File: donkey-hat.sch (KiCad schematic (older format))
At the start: 63 parts, among them J1 5V, J10 8, J11 9, J12 10, J13 11, J14 NEOPIXEL, J15 MPU-9250, J16 4, J17 5, J18 6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

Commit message: Schematic updated
PWM pins reduced.
level shifter removed.
Ultrasonic model changed.
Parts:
- removed C5, C6: 100nF, Capacitor_SMD:C_0603_1608Metric_Pad1.05x0.95mm_HandSolder, symbol Device:C
- removed J10: 8, Connector_PinHeader_2.54mm:PinHeader_1x03_P2.54mm_Vertical, symbol Connector:Conn_01x03_Male
- removed J11: 9, Connector_PinHeader_2.54mm:PinHeader_1x03_P2.54mm_Vertical, symbol Connector:Conn_01x03_Male
- removed J12: 10, Connector_PinHeader_2.54mm:PinHeader_1x03_P2.54mm_Vertical, symbol Connector:Conn_01x03_Male
- removed J13: 11, Connector_PinHeader_2.54mm:PinHeader_1x03_P2.54mm_Vertical, symbol Connector:Conn_01x03_Male
- removed J20: 12, Connector_PinHeader_2.54mm:PinHeader_1x03_P2.54mm_Vertical, symbol Connector:Conn_01x03_Male
- removed J21: 13, Connector_PinHeader_2.54mm:PinHeader_1x03_P2.54mm_Vertical, symbol Connector:Conn_01x03_Male
- removed J22: 14, Connector_PinHeader_2.54mm:PinHeader_1x03_P2.54mm_Vertical, symbol Connector:Conn_01x03_Male
- removed J23: 15, Connector_PinHeader_2.54mm:PinHeader_1x03_P2.54mm_Vertical, symbol Connector:Conn_01x03_Male
- removed J3: ULTRA_0, Connector_PinHeader_2.54mm:PinHeader_1x03_P2.54mm_Vertical, symbol Connector_Generic:Conn_01x03
- removed J4: ULTRA_1, Connector_PinHeader_2.54mm:PinHeader_1x03_P2.54mm_Vertical, symbol Connector_Generic:Conn_01x03
- removed J5: TXB0108, Package_SO:TSSOP-20_4.4x6.5mm_P0.65mm, symbol Connector_Generic:Conn_02x10_Counter_Clockwise
- removed JP10, JP11, JP12, JP13, JP8, JP9: LINK, libs:SolderJumper-2_small, symbol Jumper:SolderJumper_2_Open
- removed RN3, RN4: 220_Pack04, Resistor_SMD:R_Array_Convex_4x0603, symbol Device:R_Pack04
- added J3: ULTRA_0, Connector_PinSocket_2.54mm:PinSocket_1x04_P2.54mm_Vertical, symbol Connector_Generic:Conn_01x04
- added J4: ULTRA_1, Connector_PinSocket_2.54mm:PinSocket_1x04_P2.54mm_Vertical, symbol Connector_Generic:Conn_01x04
- added R3, R5: 330, Resistor_SMD:R_0603_1608Metric_Pad1.05x0.95mm_HandSolder, symbol Device:R
- added R4, R6: 470, Resistor_SMD:R_0603_1608Metric_Pad1.05x0.95mm_HandSolder, symbol Device:R
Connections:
- net labels added: ECHO, TRIG
- net labels removed: GPIO18_5, GPIO24_5, GPIO25_5, INT, SCL_5, SDA_5
- wire segments 366 -> 281
- no-connect marks 13 -> 7
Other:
- note added: "Accelerometer"
- moved on the sheet: J15

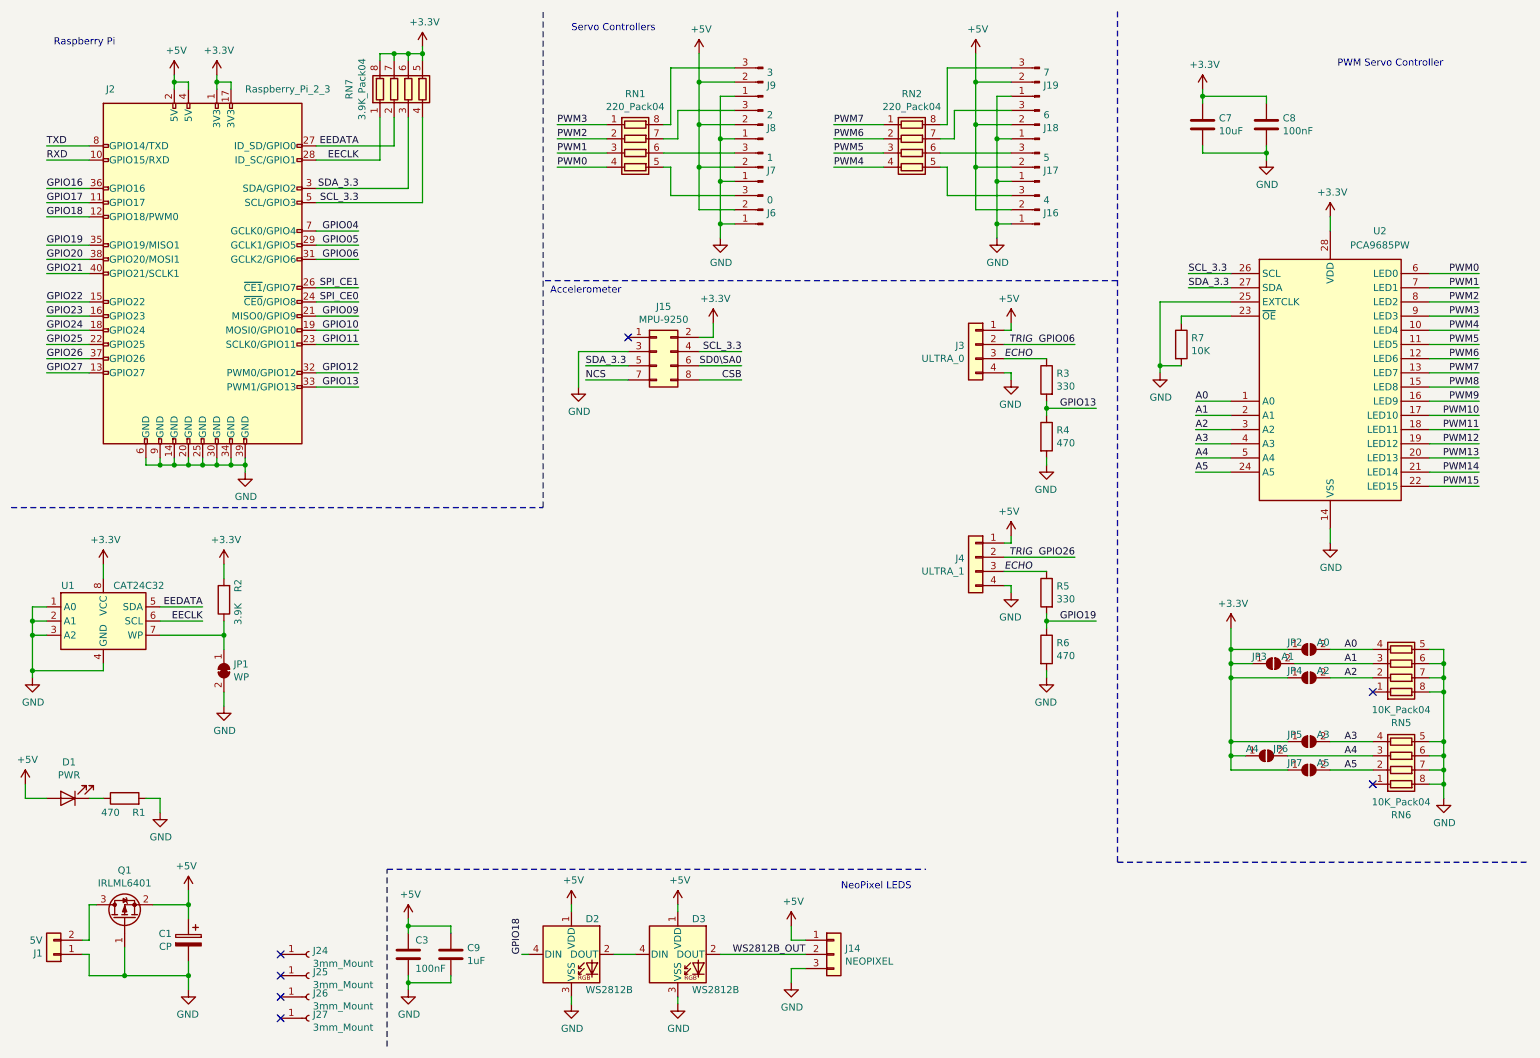
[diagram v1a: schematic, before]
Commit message: Resistor Bank for i2c is causing issues.
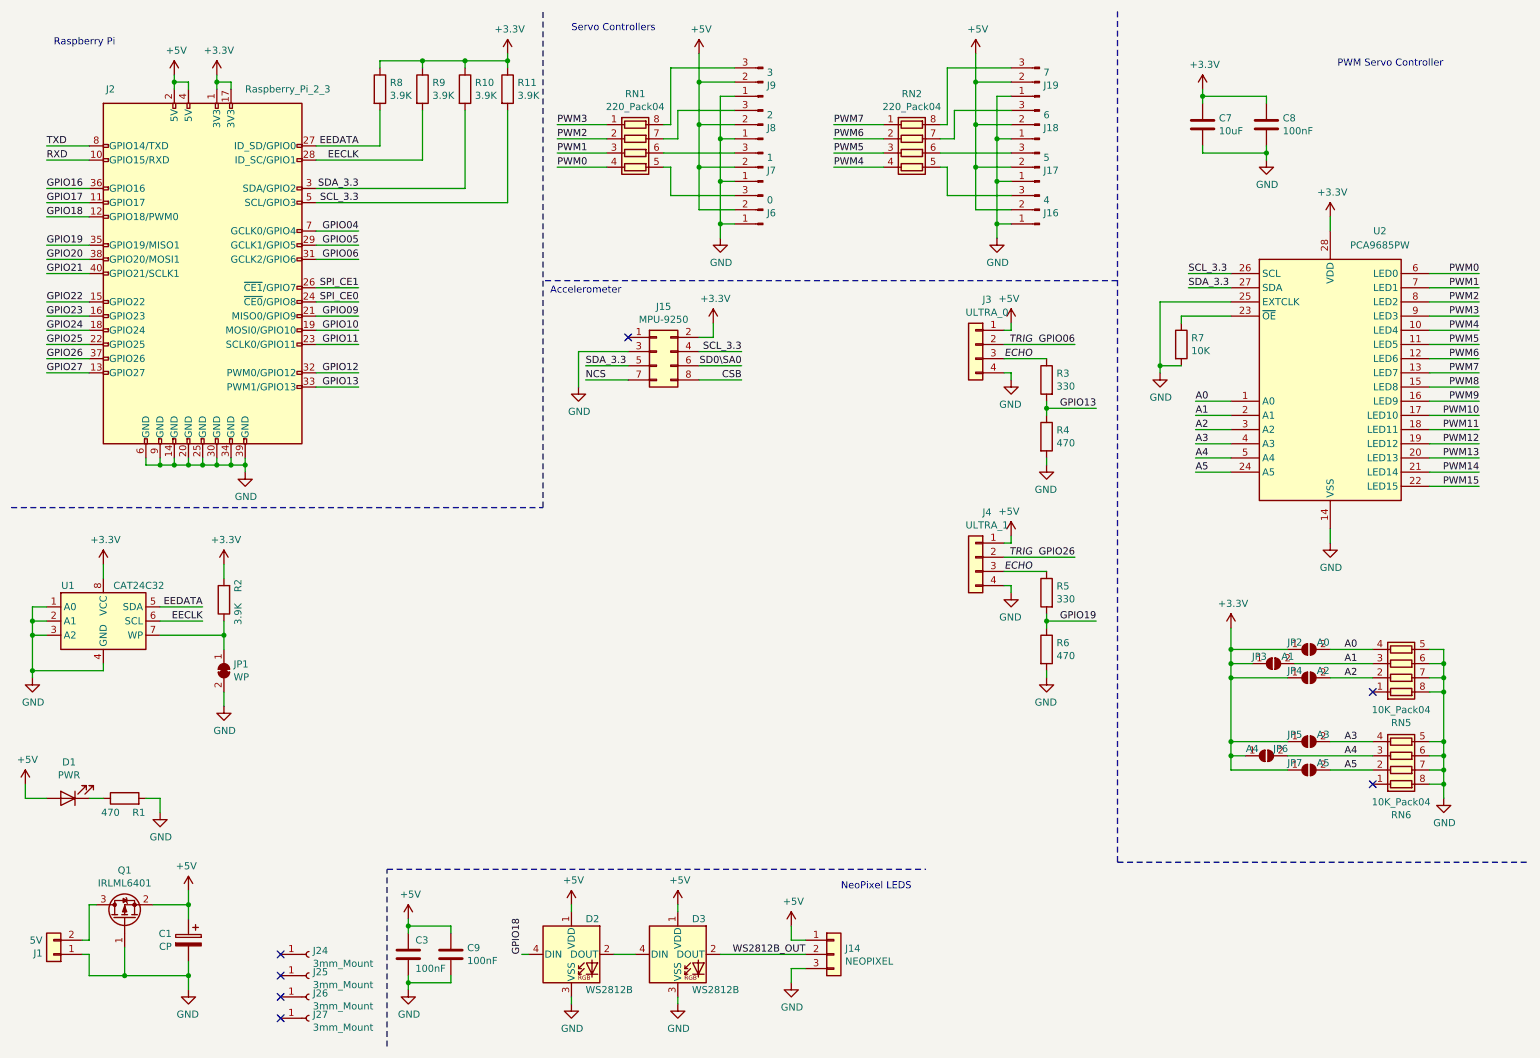
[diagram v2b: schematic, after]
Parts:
- removed RN7: 3.9K_Pack04, Resistor_SMD:R_Array_Convex_4x0603, symbol Device:R_Pack04
- added R10, R11, R8, R9: 3.9K, Resistor_SMD:R_0603_1608Metric_Pad1.05x0.95mm_HandSolder, symbol Device:R
- C9: value 1uF -> 100nF
- J3, J4: Link (none) -> https://tronixlabs.com.au/sensors/distance/ultrasonic/ultra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
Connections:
- net +3V3: now also R10.1, R11.1, R8.1, R9.1
- net EECLK: now also R9.2
- net EEDATA: now also R8.2
- net SCL_3.3: now also R11.2
- net SDA_3.3: now also R10.2
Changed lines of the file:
@@
 L power:+3.3V #PWR0111
 U 1 1 5C049CFC
-P 3400 750
-F 0 "#PWR0111" H 3400 600 50  0001 C CNN
-F 1 "+3.3V" H 3415 923 50  0000 C CNN
-F 2 "" H 3400 750 50  0001 C CNN
-F 3 "" H 3400 750 50  0001 C CNN
-	1    3400 750
+P 4000 800
+F 0 "#PWR0111" H 4000 650 50  0001 C CNN
+F 1 "+3.3V" H 4015 973 50  0000 C CNN
+F 2 "" H 4000 800 50  0001 C CNN
+F 3 "" H 4000 800 50  0001 C CNN
+	1    4000 800
 	1    0    0    -1
 $EndComp
@@
 Wire Wire Line
 	6100 7150 5500 7150
-Wire Wire Line
-	2650 1550 3100 1550
-Wire Wire Line
-	2650 1750 3300 1750
-Wire Wire Line
-	2650 1850 3400 1850
 $Comp
 L Device:C C3
@@
 A5
 $Comp
-L Device:R_Pack04 RN7
-U 1 1 5CAD6C78
-P 3300 1050
-F 0 "RN7" V 2883 1050 50  0000 C CNN
-F 1 "3.9K_Pack04" V 2974 1050 50  0000 C CNN
-F 2 "Resistor_SMD:R_Array_Convex_4x0603" V 3575 1050 50  0001 C CNN
-F 3 "~" H 3300 1050 50  0001 C CNN
-F 4 "https://www.aliexpress.com/item/200PCS-0603-2X4-220R-220-ohm-Marking-221-SMD-Network-Resistor-array-0603-8P4R-2-4P/32845505270.html?spm=2114.search0104.3.35.c74a11b9SNycSm&ws_ab_test=searchweb0_0,searchweb201602_2_10065_10068_10130_10547_319_317_10548_10696_453_10084_454_10083_10618_10307_537_536_10131_10132_10133_10059_10884_10887_100031_321_322_10103,searchweb201603_51,ppcSwitch_0&algo_expid=516fab08-5bb7-441c-804a-744d42f8303d-5&algo_pvid=516fab08-5bb7-441c-804a-744d42f8303d" V 3300 1050 50  0001 C CNN "Link"
-	1    3300 1050
-	1    0    0    -1
-$EndComp
-Wire Wire Line
-	3100 850  3100 800
-Wire Wire Line
-	3100 800  3200 800
-Wire Wire Line
-	3400 800  3400 750
-Wire Wire Line
-	3400 850  3400 800
-Connection ~ 3400 800
-Wire Wire Line
-	3300 850  3300 800
-Connection ~ 3300 800
-Wire Wire Line
-	3300 800  3400 800
-Wire Wire Line
-	3200 850  3200 800
-Connection ~ 3200 800
-Wire Wire Line
-	3200 800  3300 800
-Wire Wire Line
-	3300 1250 3300 1750
-Wire Wire Line
-	3400 1250 3400 1850
-$Comp
 L Device:C C9
 U 1 1 5CC83074
 P 3600 7150
 F 0 "C9" H 3715 7196 50  0000 L CNN
-F 1 "1uF" H 3715 7105 50  0000 L CNN
+F 1 "100nF" H 3715 7105 50  0000 L CNN
 F 2 "Capacitor_SMD:C_0603_1608Metric_Pad1.05x0.95mm_HandSolder" H 3638 7000 50  0001 C CNN
 F 3 "~" H 3600 7150 50  0001 C CNN
@@
 	3300 7350 3300 7300
 Wire Wire Line
-	3200 1450 3200 1250
-Wire Wire Line
-	2650 1450 3200 1450
-Wire Wire Line
-	3100 1250 3100 1550
+	2650 1450 3100 1450
 $Comp
 L Connector_Generic:Conn_02x04_Odd_Even J15
@@
 U 1 1 5C1BDC5B
 P 7300 4350
-F 0 "J4" H 7379 4342 50  0000 L CNN
-F 1 "ULTRA_1" H 7379 4251 50  0000 L CNN
+F 0 "J4" H 7220 4667 50  0000 C CNN
+F 1 "ULTRA_1" H 7220 4576 50  0000 C CNN
 F 2 "Connector_PinSocket_2.54mm:PinSocket_1x04_P2.54mm_Vertical" H 7300 4350 50  0001 C CNN
 F 3 "~" H 7300 4350 50  0001 C CNN
+F 4 "https://tronixlabs.com.au/sensors/distance/ultrasonic/ultrasonic-distance-sensor-module-hc-sr04-2-450-cm-australia/" H 7300 4350 50  0001 C CNN "Link"
 	1    7300 4350
 	-1   0    0    -1
@@
 U 1 1 5C210D5B
 P 7300 2850
-F 0 "J3" H 7379 2842 50  0000 L CNN
-F 1 "ULTRA_0" H 7379 2751 50  0000 L CNN
+F 0 "J3" H 7220 3167 50  0000 C CNN
+F 1 "ULTRA_0" H 7220 3076 50  0000 C CNN
 F 2 "Connector_PinSocket_2.54mm:PinSocket_1x04_P2.54mm_Vertical" H 7300 2850 50  0001 C CNN
 F 3 "~" H 7300 2850 50  0001 C CNN
+F 4 "https://tronixlabs.com.au/sensors/distance/ultrasonic/ultrasonic-distance-sensor-module-hc-sr04-2-450-cm-australia/" H 7300 2850 50  0001 C CNN "Link"
 	1    7300 2850
 	-1   0    0    -1
@@
 Wire Wire Line
 	7800 5200 7800 5150
+$Comp
+L Device:R R8
+U 1 1 5C3CDDE7
+P 3100 1050
+F 0 "R8" H 3170 1096 50  0000 L CNN
+F 1 "3.9K" H 3170 1005 50  0000 L CNN
+F 2 "Resistor_SMD:R_0603_1608Metric_Pad1.05x0.95mm_HandSolder" V 3030 1050 50  0001 C CNN
+F 3 "~" H 3100 1050 50  0001 C CNN
+	1    3100 1050
+	1    0    0    -1
+$EndComp
+$Comp
+L Device:R R9
+U 1 1 5C40A918
+P 3400 1050
+F 0 "R9" H 3470 1096 50  0000 L CNN
+F 1 "3.9K" H 3470 1005 50  0000 L CNN
+F 2 "Resistor_SMD:R_0603_1608Metric_Pad1.05x0.95mm_HandSolder" V 3330 1050 50  0001 C CNN
+F 3 "~" H 3400 1050 50  0001 C CNN
+	1    3400 1050
+	1    0    0    -1
+$EndComp
+$Comp
+L Device:R R10
+U 1 1 5C432542
+P 3700 1050
+F 0 "R10" H 3770 1096 50  0000 L CNN
+F 1 "3.9K" H 3770 1005 50  0000 L CNN
+F 2 "Resistor_SMD:R_0603_1608Metric_Pad1.05x0.95mm_HandSolder" V 3630 1050 50  0001 C CNN
+F 3 "~" H 3700 1050 50  0001 C CNN
+	1    3700 1050
+	1    0    0    -1
+$EndComp
+$Comp
+L Device:R R11
+U 1 1 5C432548
+P 4000 1050
+F 0 "R11" H 4070 1096 50  0000 L CNN
+F 1 "3.9K" H 4070 1005 50  0000 L CNN
+F 2 "Resistor_SMD:R_0603_1608Metric_Pad1.05x0.95mm_HandSolder" V 3930 1050 50  0001 C CNN
+F 3 "~" H 4000 1050 50  0001 C CNN
+	1    4000 1050
+	1    0    0    -1
+$EndComp
+Wire Wire Line
+	3400 1550 3400 1200
+Wire Wire Line
+	2650 1550 3400 1550
+Wire Wire Line
+	3100 1450 3100 1200
+Wire Wire Line
+	3100 900  3100 850
+Wire Wire Line
+	3100 850  3400 850
+Wire Wire Line
+	4000 850  4000 900
+Wire Wire Line
+	3400 900  3400 850
+Connection ~ 3400 850
+Wire Wire Line
+	3400 850  3700 850
+Wire Wire Line
+	3700 850  3700 900
+Connection ~ 3700 850
+Wire Wire Line
+	3700 850  4000 850
+Wire Wire Line
+	3700 1200 3700 1750
+Wire Wire Line
+	2650 1750 3700 1750
+Wire Wire Line
+	4000 1850 4000 1200
+Wire Wire Line
+	2650 1850 4000 1850
+Wire Wire Line
+	4000 800  4000 850
+Connection ~ 4000 850
 $EndSCHEMATC

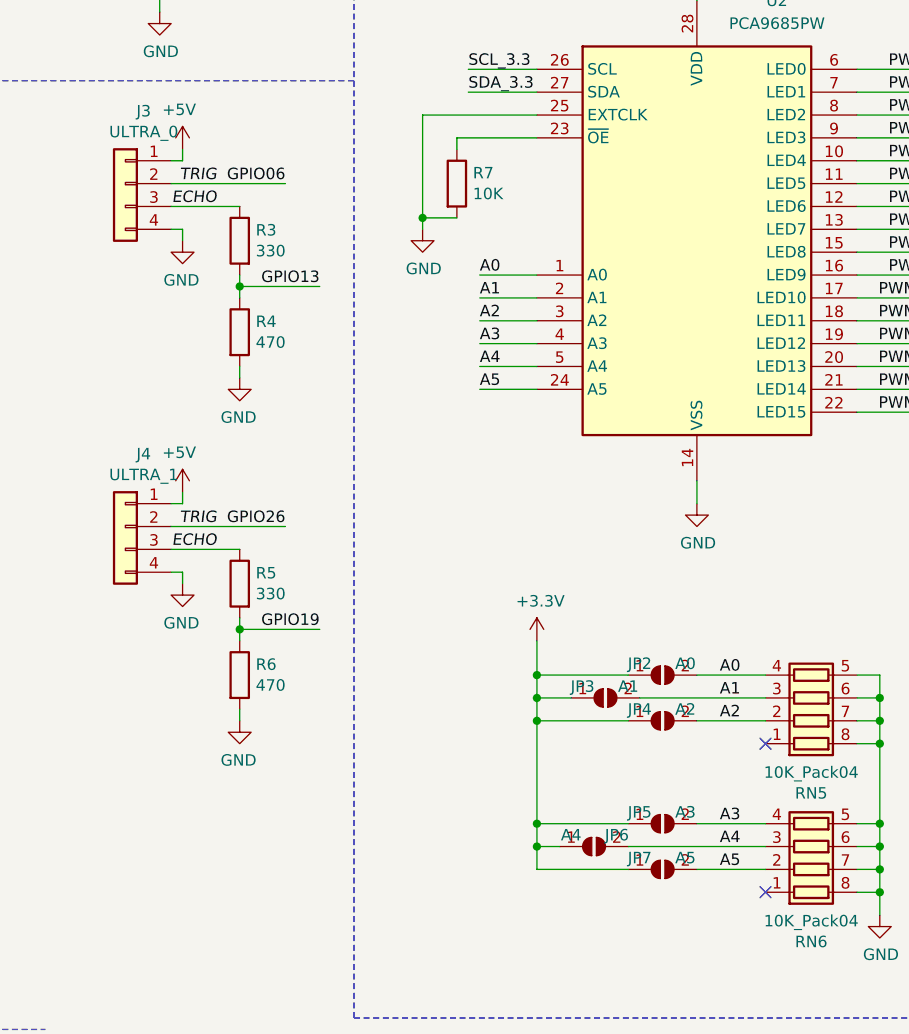
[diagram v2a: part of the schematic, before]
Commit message: New PCB to take in to account schematic changes
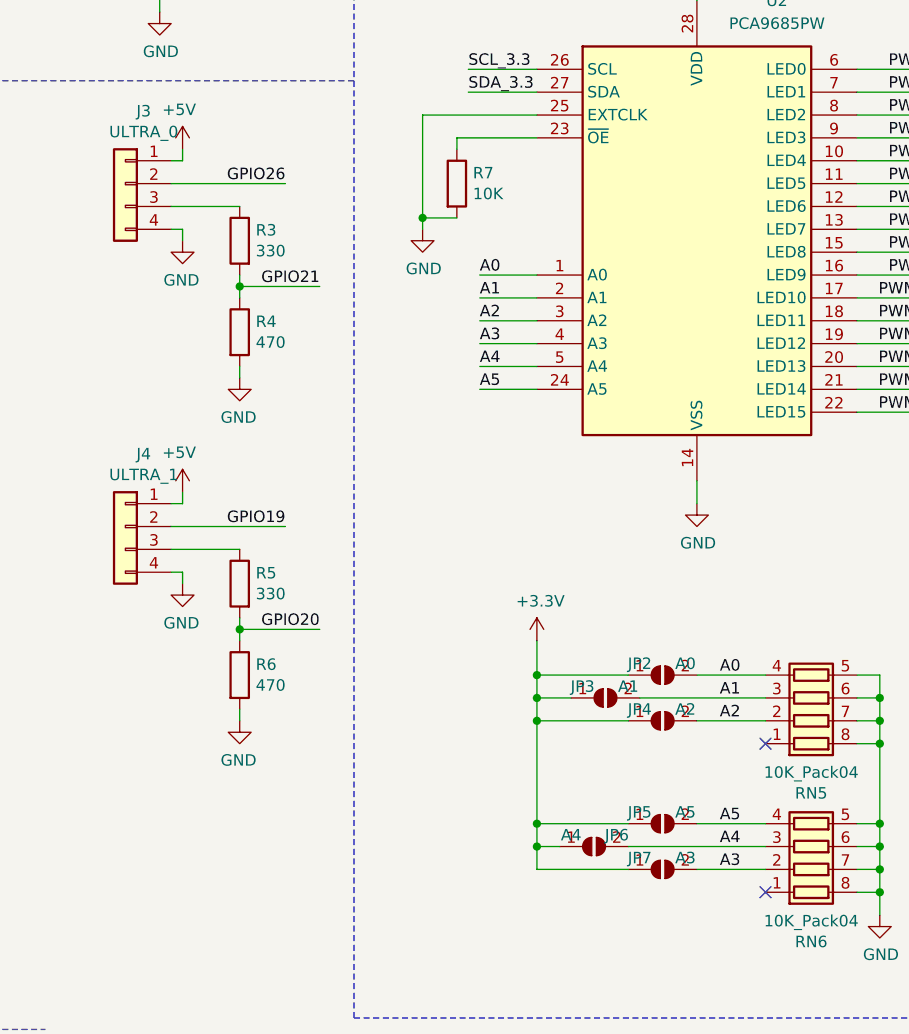
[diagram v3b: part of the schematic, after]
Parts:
- JP5: value A3 -> A5
- JP7: value A5 -> A3
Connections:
- net A3: now also JP7.2 (B), RN6.2 (R2.1); no longer JP5.2 (B), RN6.4 (R4.1)
- net A5: now also JP5.2 (B), RN6.4 (R4.1); no longer JP7.2 (B), RN6.2 (R2.1)
- net GPIO06: no longer J2.37 (GPIO26), J3.2 (Pin_2), J4.2 (Pin_2)
- net GPIO13: no longer R3.2, R4.1
- net GPIO19: now also J4.2 (Pin_2); no longer R5.2, R6.1
- net GPIO20: now also R5.2, R6.1
- net GPIO21: now also R3.2, R4.1
- net ECHO: no longer names the net of J4.3 (Pin_3), R5.1
- net ECHO: no longer J3.3 (Pin_3), R3.1
- new net: J3.3 (Pin_3), R3.1
- new net GPIO26: J2.37 (GPIO26), J3.2 (Pin_2)
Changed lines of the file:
@@
 P 9650 5650
 F 0 "JP5" H 9550 5700 50  0000 C CNN
-F 1 "A3" H 9750 5700 50  0000 C CNN
+F 1 "A5" H 9750 5700 50  0000 C CNN
 F 2 "Jumper:SolderJumper-2_P1.3mm_Open_RoundedPad1.0x1.5mm" H 9650 5650 50  0001 C CNN
 F 3 "~" H 9650 5650 50  0001 C CNN
@@
 P 9650 5850
 F 0 "JP7" H 9550 5900 50  0000 C CNN
-F 1 "A5" H 9750 5900 50  0000 C CNN
+F 1 "A3" H 9750 5900 50  0000 C CNN
 F 2 "Jumper:SolderJumper-2_P1.3mm_Open_RoundedPad1.0x1.5mm" H 9650 5850 50  0001 C CNN
 F 3 "~" H 9650 5850 50  0001 C CNN
@@
 Text Label 9900 5200 0    50   ~ 0
 A2
-Text Label 9900 5650 0    50   ~ 0
+Text Label 9900 5850 0    50   ~ 0
 A3
 Text Label 9900 5750 0    50   ~ 0
 A4
-Text Label 9900 5850 0    50   ~ 0
+Text Label 9900 5650 0    50   ~ 0
 A5
 $Comp
@@
 Wire Wire Line
 	7500 4450 7800 4450
-Text Label 7700 4450 2    50   Italic 0
-ECHO
-Text Label 7700 4350 2    50   Italic 0
-TRIG
 Wire Wire Line
 	7500 4350 8000 4350
@@
 Wire Wire Line
 	7500 2950 7800 2950
-Text Label 7700 2950 2    50   Italic 0
-ECHO
-Text Label 7700 2850 2    50   Italic 0
-TRIG
 Wire Wire Line
 	7500 2850 8000 2850
@@
 Wire Wire Line
 	7550 3050 7500 3050
-Text Label 8000 2850 2    50   ~ 0
-GPIO06
-Text Label 8150 4800 2    50   ~ 0
+Text Label 8000 4350 2    50   ~ 0
 GPIO19
 Text Label 8150 3300 2    50   ~ 0
-GPIO13
-Text Label 8000 4350 2    50   ~ 0
+GPIO21
+Text Label 8150 4800 2    50   ~ 0
+GPIO20
+Text Label 8000 2850 2    50   ~ 0
 GPIO26
 $Comp
